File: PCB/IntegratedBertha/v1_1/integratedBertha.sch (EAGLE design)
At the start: 100 parts, among them CON1 SPI, IC1 REG1117, IC2 AD8223, J7 22--02, Q1 BSP75, Q2 BSP75, Q4 BSP75, Q5 BSP75, Q6 BSP75, Q7 IRF3704S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

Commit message: integratedBertha v1.1: adjusted labels to good position. Anemometer: added ferrite bead for vcc decoupling and ground line.
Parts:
- renumbered LED1 to BLINK, LED10 to 12V-OK, LED3 to 3.3V-OK, LED4 to 5V-OK
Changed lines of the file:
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@@
 <part name="LED2" library="adafruit" deviceset="LED" device="CHIPLED_1206" value="Blue"/>
 <part name="R25" library="rcl" deviceset="R-EU_" device="R0805" value="1k"/>
-<part name="LED3" library="adafruit" deviceset="LED" device="CHIPLED_1206" value="RED"/>
+<part name="3.3V-OK" library="adafruit" deviceset="LED" device="CHIPLED_1206" value="RED"/>
 <part name="R27" library="rcl" deviceset="R-EU_" device="R0805" value="1K"/>
 <part name="C5" library="rcl" deviceset="C-EU" device="C1206" value="10uF"/>
@@
 <part name="R7" library="rcl" deviceset="R-EU_" device="R0805" value="1k"/>
 <part name="U$6" library="lpatiny" deviceset="KPJX-4S-S" device="" value="KPJX-4S-S"/>
-<part name="LED10" library="adafruit" deviceset="LED" device="CHIPLED_1206" value="RED"/>
+<part name="12V-OK" library="adafruit" deviceset="LED" device="CHIPLED_1206" value="RED"/>
 <part name="RL3" library="rcl" deviceset="R-EU_" device="R0805" value="1K"/>
 <part name="P+17" library="supply1" deviceset="+12V" device=""/>
@@
 <part name="C10" library="rcl" deviceset="C-EU" device="C1206" value="10uF"/>
 <part name="D2" library="lpatiny" deviceset="1N581*" device="D1206" value="1N581D1206"/>
-<part name="LED4" library="adafruit" deviceset="LED" device="CHIPLED_1206" value="RED"/>
+<part name="5V-OK" library="adafruit" deviceset="LED" device="CHIPLED_1206" value="RED"/>
 <part name="RL4" library="resistor" deviceset="R-EU_" device="R0805" value="1K"/>
 <part name="D3" library="lpatiny" deviceset="1N581*" device="D1206" value="1N581D1206"/>
@@
 <part name="RL5" library="rcl" deviceset="R-EU_" device="R0805" value="1K"/>
 <part name="GND21" library="supply2" deviceset="DGND" device=""/>
-<part name="LED1" library="adafruit" deviceset="LED" device="CHIPLED_1206" value="GREEN"/>
+<part name="BLINK" library="adafruit" deviceset="LED" device="CHIPLED_1206" value="GREEN"/>
 <part name="+5VA4" library="supply1" deviceset="+5V" device=""/>
 <part name="+5VA5" library="supply1" deviceset="+5V" device=""/>
@@
 <instance part="LED2" gate="G$1" x="58.42" y="266.7" rot="R270"/>
 <instance part="R25" gate="G$1" x="60.96" y="274.32" rot="R90"/>
-<instance part="LED3" gate="G$1" x="-71.12" y="274.32" rot="MR0"/>
+<instance part="3.3V-OK" gate="G$1" x="-71.12" y="274.32" rot="MR0"/>
 <instance part="R27" gate="G$1" x="-71.12" y="284.48" rot="MR90"/>
 <instance part="C5" gate="G$1" x="-114.3" y="292.1"/>
@@
 <instance part="R7" gate="G$1" x="233.68" y="279.4" rot="R90"/>
 <instance part="U$6" gate="G$1" x="2.54" y="286.004"/>
-<instance part="LED10" gate="G$1" x="-35.56" y="281.94" rot="MR90"/>
+<instance part="12V-OK" gate="G$1" x="-35.56" y="281.94" rot="MR90"/>
 <instance part="RL3" gate="G$1" x="-27.94" y="281.94" rot="MR180"/>
 <instance part="P+17" gate="1" x="-20.32" y="274.32" smashed="yes" rot="R180">
@@
 <instance part="C10" gate="G$1" x="276.86" y="147.32"/>
 <instance part="D2" gate="G$1" x="248.92" y="162.56"/>
-<instance part="LED4" gate="G$1" x="302.26" y="147.32" rot="MR0"/>
+<instance part="5V-OK" gate="G$1" x="302.26" y="147.32" rot="MR0"/>
 <instance part="RL4" gate="G$1" x="294.64" y="149.86" rot="MR180"/>
 <instance part="D3" gate="G$1" x="248.92" y="149.86"/>
@@
 <attribute name="VALUE" x="-4.445" y="257.175" size="1.27" layer="96"/>
 </instance>
-<instance part="LED1" gate="G$1" x="10.16" y="256.54" rot="R180"/>
+<instance part="BLINK" gate="G$1" x="10.16" y="256.54" rot="R180"/>
 <instance part="+5VA4" gate="1" x="38.1" y="93.98"/>
 <instance part="+5VA5" gate="1" x="38.1" y="73.66"/>
@@
 <wire x1="10.16" y1="261.62" x2="-2.54" y2="261.62" width="0.1524" layer="91"/>
 <pinref part="GND21" gate="G$1" pin="DGND"/>
-<pinref part="LED1" gate="G$1" pin="C"/>
+<pinref part="BLINK" gate="G$1" pin="C"/>
 <junction x="10.16" y="261.62"/>
 <junction x="-2.54" y="261.62"/>
@@
 <wire x1="271.78" y1="142.24" x2="276.86" y2="142.24" width="0.1524" layer="91"/>
 <junction x="276.86" y="142.24"/>
-<pinref part="LED4" gate="G$1" pin="C"/>
+<pinref part="5V-OK" gate="G$1" pin="C"/>
 <wire x1="302.26" y1="142.24" x2="284.48" y2="142.24" width="0.1524" layer="91"/>
 <pinref part="C12" gate="G$1" pin="1"/>
@@
 <wire x1="-40.64" y1="281.94" x2="-40.64" y2="287.02" width="0.1524" layer="91"/>
 <pinref part="U$6" gate="G$1" pin="GND1"/>
-<pinref part="LED10" gate="G$1" pin="C"/>
+<pinref part="12V-OK" gate="G$1" pin="C"/>
 <pinref part="DGND15" gate="G$1" pin="DGND"/>
 <junction x="-40.64" y="287.02"/>
 </segment>
 <segment>
-<pinref part="LED3" gate="G$1" pin="C"/>
+<pinref part="3.3V-OK" gate="G$1" pin="C"/>
 <wire x1="-71.12" y1="269.24" x2="-71.12" y2="266.7" width="0.1524" layer="91"/>
 <pinref part="DGND14" gate="G$1" pin="DGND"/>
@@
 <wire x1="-71.12" y1="279.4" x2="-71.12" y2="276.86" width="0.1524" layer="91"/>
 <pinref part="R27" gate="G$1" pin="1"/>
-<pinref part="LED3" gate="G$1" pin="A"/>
+<pinref part="3.3V-OK" gate="G$1" pin="A"/>
 </segment>
 </net>
@@
 <net name="N$75" class="0">
 <segment>
-<pinref part="LED10" gate="G$1" pin="A"/>
+<pinref part="12V-OK" gate="G$1" pin="A"/>
 <pinref part="RL3" gate="G$1" pin="1"/>
 </segment>
@@
 <segment>
 <pinref part="RL4" gate="G$1" pin="2"/>
-<pinref part="LED4" gate="G$1" pin="A"/>
+<pinref part="5V-OK" gate="G$1" pin="A"/>
 <wire x1="299.72" y1="149.86" x2="302.26" y2="149.86" width="0.1524" layer="91"/>
 </segment>
@@
 <pinref part="RL5" gate="G$1" pin="2"/>
 <wire x1="10.16" y1="254" x2="0" y2="254" width="0.1524" layer="91"/>
-<pinref part="LED1" gate="G$1" pin="A"/>
+<pinref part="BLINK" gate="G$1" pin="A"/>
 <junction x="10.16" y="254"/>
 </segment>

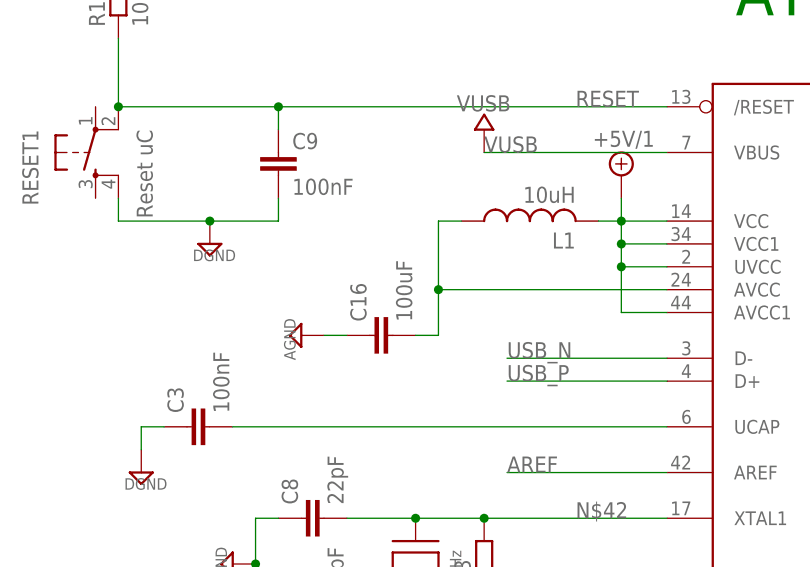
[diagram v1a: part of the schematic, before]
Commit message: changed some labels, corrected C16 value in bertha. created BOM
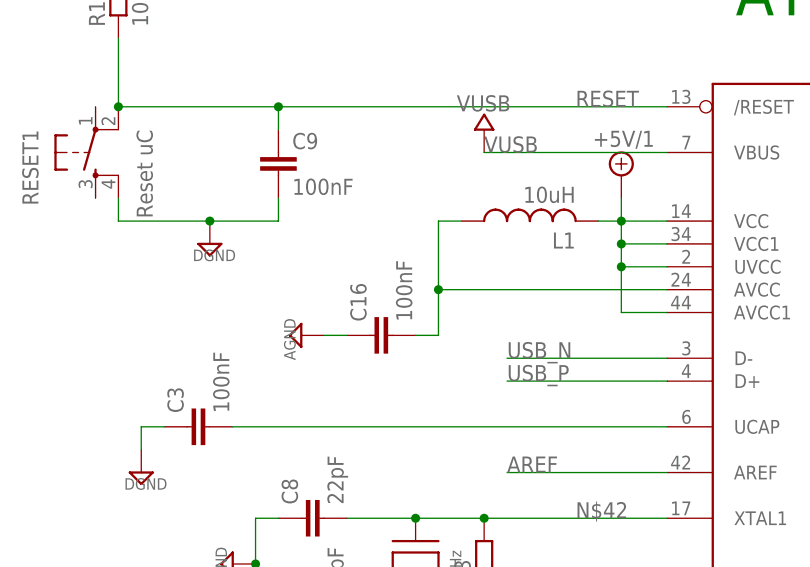
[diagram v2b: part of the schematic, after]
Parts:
- C16: value 100uF -> 100nF
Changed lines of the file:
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@@
 <part name="AGND3" library="supply2" deviceset="AGND" device="" value="AGND"/>
 <part name="AGND4" library="supply2" deviceset="AGND" device="" value="AGND"/>
-<part name="C16" library="rcl" deviceset="C-EU" device="C1206" value="100uF"/>
+<part name="C16" library="rcl" deviceset="C-EU" device="C1206" value="100nF"/>
 <part name="L1" library="rcl" deviceset="L-US" device="L2012C" value="10uH"/>
 <part name="AGND6" library="supply2" deviceset="AGND" device="" value="AGND"/>
